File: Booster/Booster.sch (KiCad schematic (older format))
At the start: 1 part, among them J101 Track

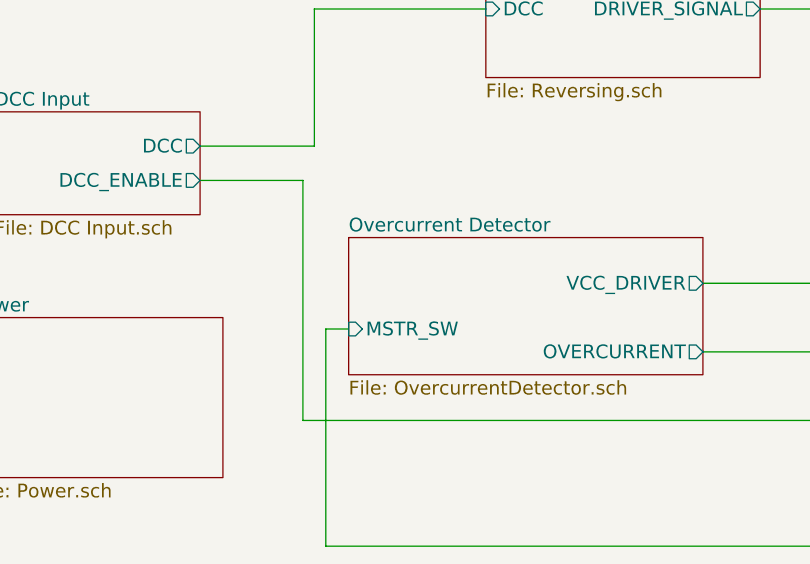
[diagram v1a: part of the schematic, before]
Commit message: Replaced NAND gate with AND as the additional NOT gates ended up only used to negate the NAND gates directly. One extra AND gate used to allow resetting overcurrent by either master switch or DCC disable/enable.
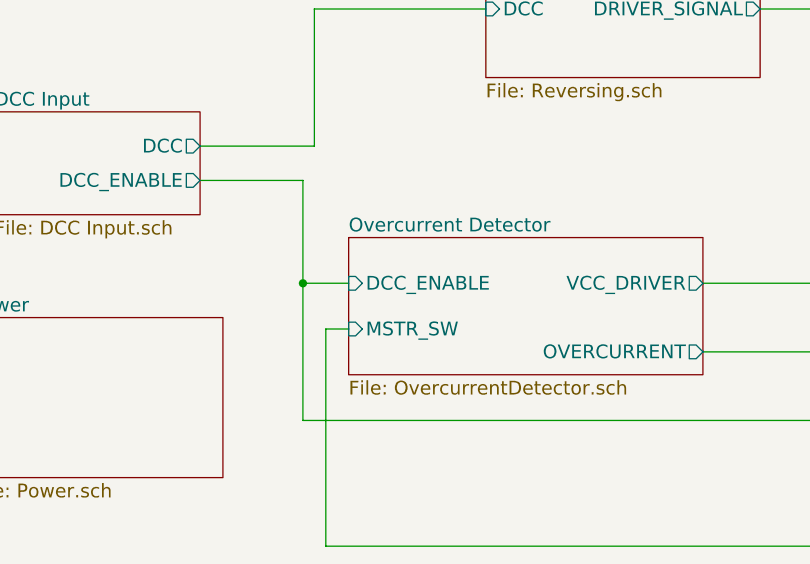
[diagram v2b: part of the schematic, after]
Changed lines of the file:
@@
 F3 "OVERCURRENT" O R 4400 5000 60
 F4 "MSTR_SW" I L 2850 4900 60
+F5 "DCC_ENABLE" I L 2850 4700 60
 $EndSheet
 $Sheet
@@
 Wire Wire Line
 	10050 4100 9800 4100
+Wire Wire Line
+	2850 4700 2650 4700
+Connection ~ 2650 4700
 $EndSCHEMATC

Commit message: Assigned footprints & minor adjustments.
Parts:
- J101: footprint (none) -> Connectors_Terminal_Blocks:TerminalBlock_bornier-2_P5.08mm
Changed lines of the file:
@@
 F 0 "J101" H 10500 4250 50  0000 C CNN
 F 1 "Track" H 10500 3950 50  0000 C CNN
-F 2 "" H 10500 4150 50  0001 C CNN
+F 2 "Connectors_Terminal_Blocks:TerminalBlock_bornier-2_P5.08mm" H 10500 4150 50  0001 C CNN
 F 3 "" H 10500 4150 50  0001 C CNN
 	1    10500 4150
